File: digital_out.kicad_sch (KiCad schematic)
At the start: 2 parts, among them U5 AM26LS31

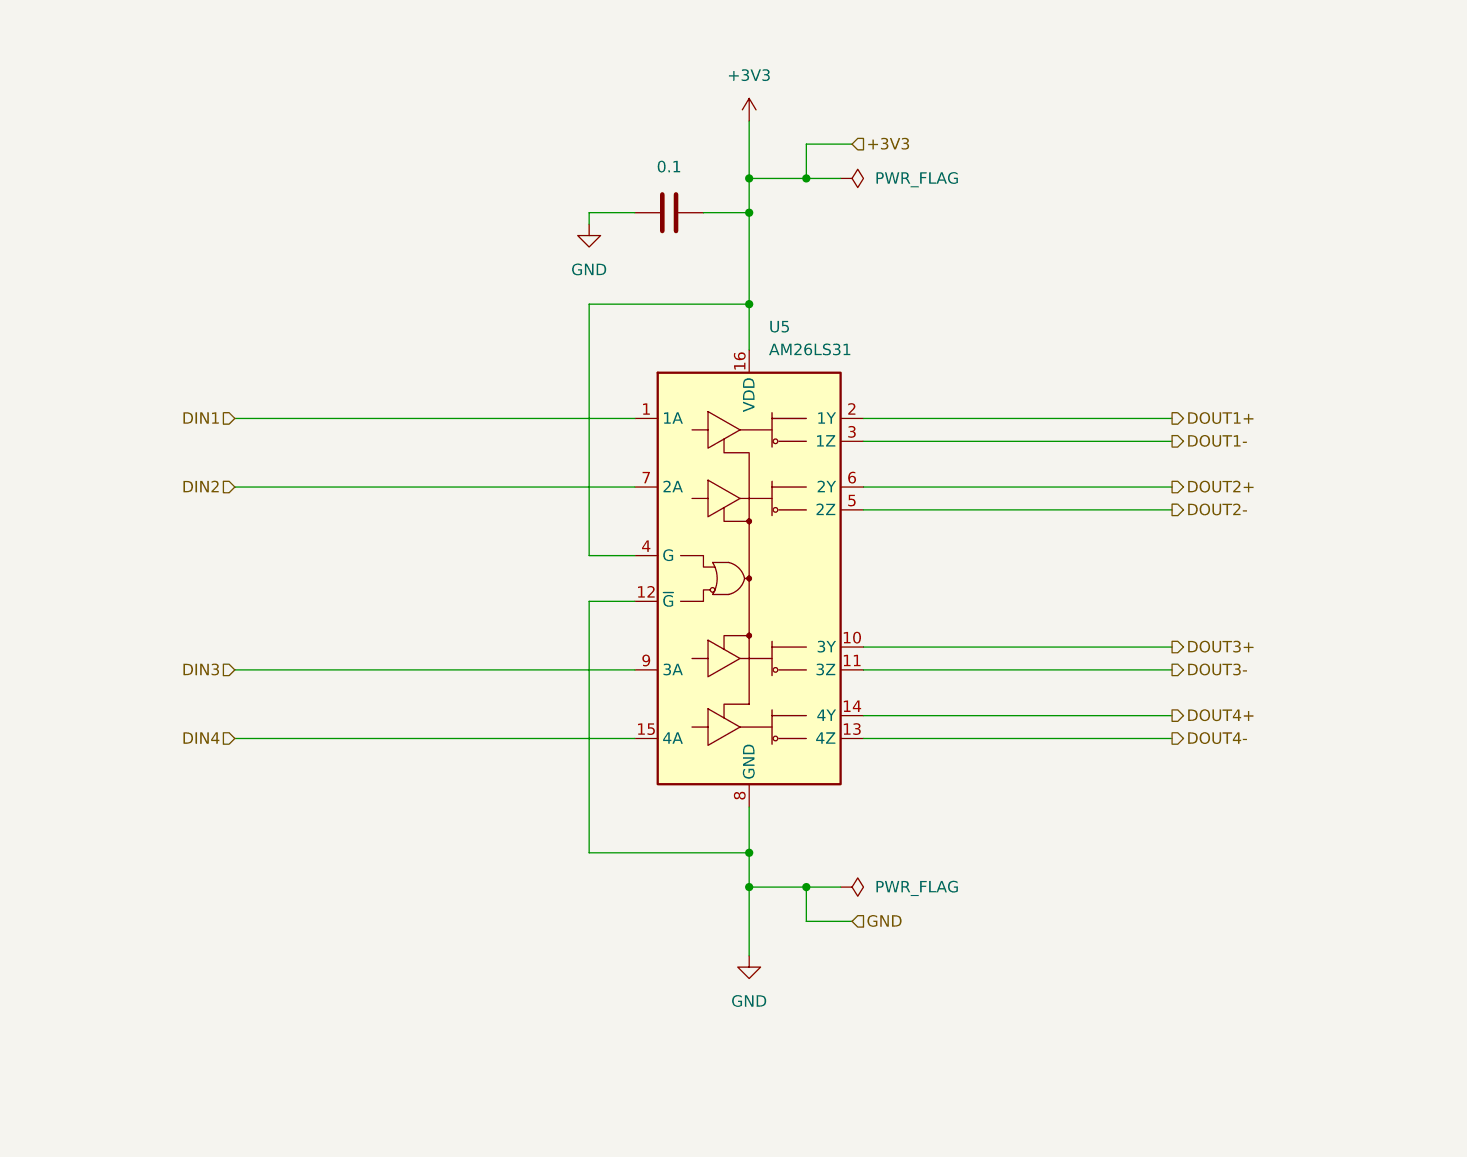
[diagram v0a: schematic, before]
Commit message: Finished power setup and cleared some mistakes
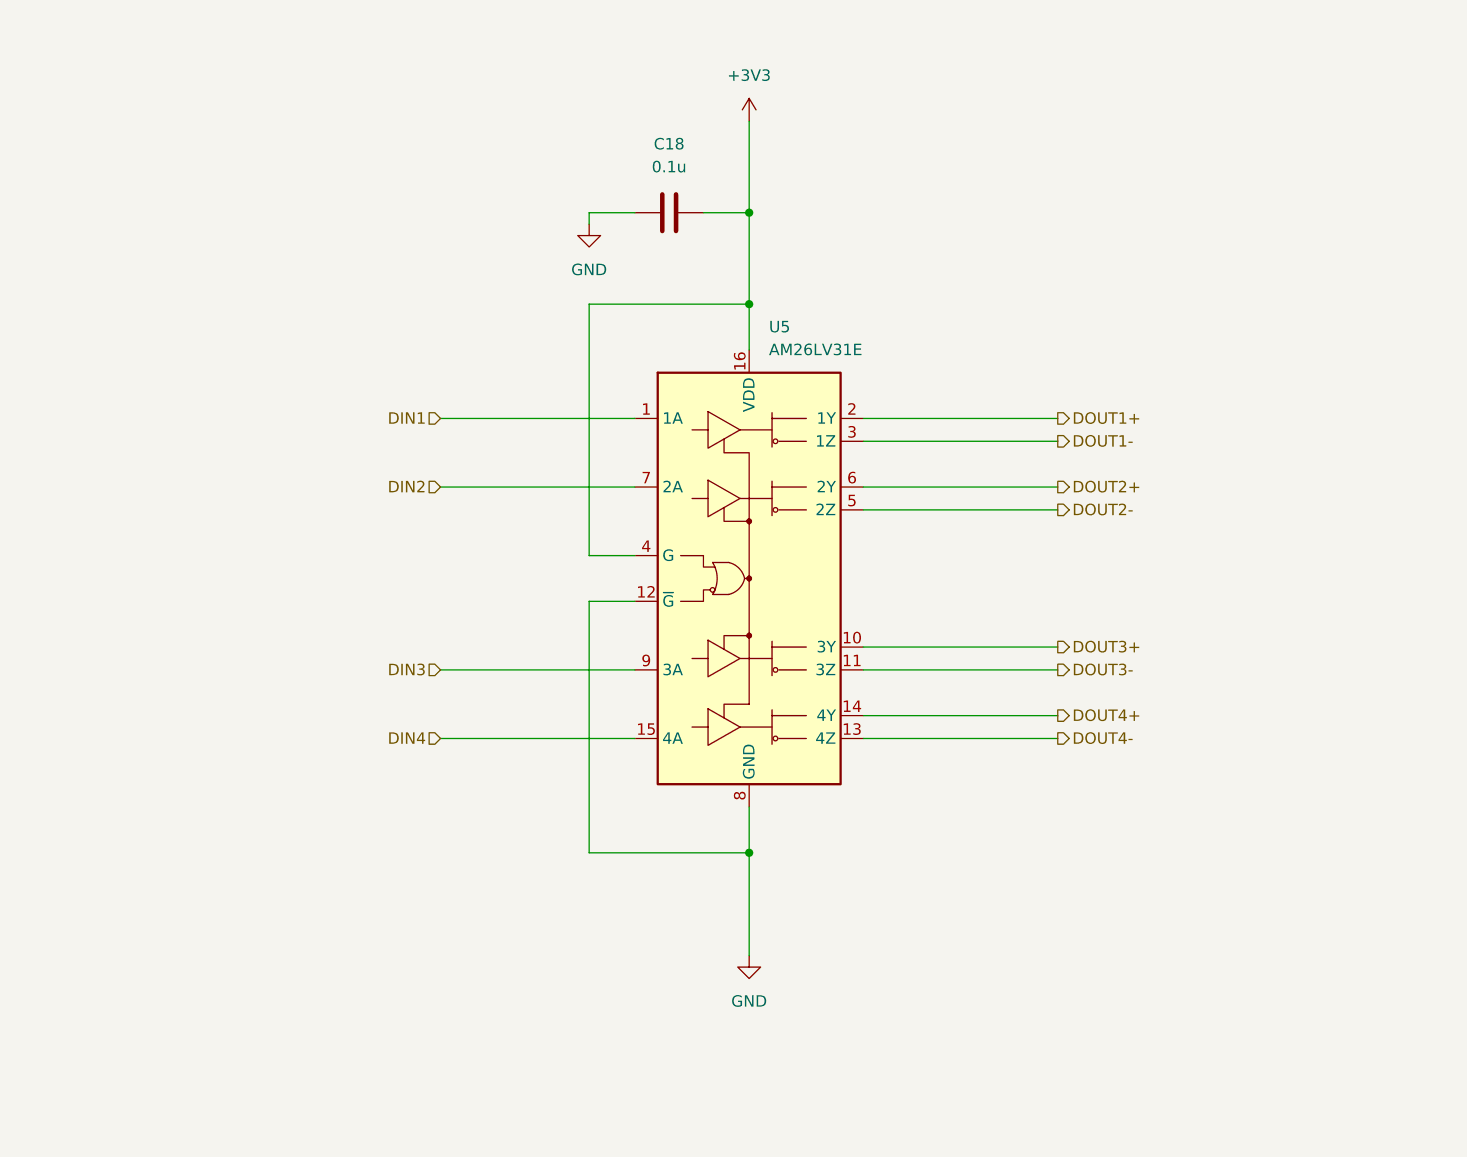
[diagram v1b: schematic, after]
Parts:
- C18: value 0.1 -> 0.1u
- U5: value AM26LS31 -> AM26LV31E

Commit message: Assigned proper footprints for all components
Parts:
- C18: value 0.1u -> 100n; footprint (none) -> Capacitor_SMD:C_0603_1608Metric_Pad1.08x0.95mm_HandSolder
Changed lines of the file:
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@@
       (effects (font (size 1.27 1.27)))
     )
-    (property "Value" "0.1u" (at 146.05 45.72 90)
+    (property "Value" "100n" (at 146.05 45.72 90)
       (effects (font (size 1.27 1.27)))
     )
-    (property "Footprint" "" (at 149.86 49.8348 0)
+    (property "Footprint" "Capacitor_SMD:C_0603_1608Metric_Pad1.08x0.95mm_HandSolder" (at 149.86 49.8348 0)
       (effects (font (size 1.27 1.27)) hide)
     )

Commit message: Finished annotation
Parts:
- renumbered C18 to C2601, U5 to U2601
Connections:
- net DOUT1+ renamed DIN1+
- net DOUT1- renamed DIN1-
- net DOUT2+ renamed DIN2+
- net DOUT2- renamed DIN2-
- net DOUT3+ renamed DIN3+
- net DOUT3- renamed DIN3-
- net DOUT4+ renamed DIN4+
- net DOUT4- renamed DIN4-

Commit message: Merged receiver and transmitter
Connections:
- net DIN1 renamed DOUT1
- net DIN1+ renamed DOUT1+
- net DIN1- renamed DOUT1-
- net DIN2 renamed DOUT2
- net DIN2+ renamed DOUT2+
- net DIN2- renamed DOUT2-
- net DIN3 renamed DOUT3
- net DIN3+ renamed DOUT3+
- net DIN3- renamed DOUT3-
- net DIN4 renamed DOUT4
- net DIN4+ renamed DOUT4+
- net DIN4- renamed DOUT4-
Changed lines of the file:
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@@
     (stroke (width 0) (type default))
   )
-  (hierarchical_label "DIN3-" (shape output) (at 189.23 101.6 0) (fields_autoplaced)
+  (hierarchical_label "DOUT3-" (shape output) (at 189.23 101.6 0) (fields_autoplaced)
     (effects (font (size 1.27 1.27)) (justify left))
   )
-  (hierarchical_label "DIN1-" (shape output) (at 189.23 76.2 0) (fields_autoplaced)
+  (hierarchical_label "DOUT1-" (shape output) (at 189.23 76.2 0) (fields_autoplaced)
     (effects (font (size 1.27 1.27)) (justify left))
   )
-  (hierarchical_label "DIN4" (shape input) (at 120.65 109.22 180) (fields_autoplaced)
+  (hierarchical_label "DOUT4" (shape input) (at 120.65 109.22 180) (fields_autoplaced)
     (effects (font (size 1.27 1.27)) (justify right))
   )
-  (hierarchical_label "DIN2-" (shape output) (at 189.23 83.82 0) (fields_autoplaced)
+  (hierarchical_label "DOUT2-" (shape output) (at 189.23 83.82 0) (fields_autoplaced)
     (effects (font (size 1.27 1.27)) (justify left))
   )
-  (hierarchical_label "DIN3" (shape input) (at 120.65 101.6 180) (fields_autoplaced)
+  (hierarchical_label "DOUT3" (shape input) (at 120.65 101.6 180) (fields_autoplaced)
     (effects (font (size 1.27 1.27)) (justify right))
   )
-  (hierarchical_label "DIN4+" (shape output) (at 189.23 106.68 0) (fields_autoplaced)
+  (hierarchical_label "DOUT4+" (shape output) (at 189.23 106.68 0) (fields_autoplaced)
     (effects (font (size 1.27 1.27)) (justify left))
   )
-  (hierarchical_label "DIN3+" (shape output) (at 189.23 99.06 0) (fields_autoplaced)
+  (hierarchical_label "DOUT3+" (shape output) (at 189.23 99.06 0) (fields_autoplaced)
     (effects (font (size 1.27 1.27)) (justify left))
   )
-  (hierarchical_label "DIN2" (shape input) (at 120.65 81.28 180) (fields_autoplaced)
+  (hierarchical_label "DOUT2" (shape input) (at 120.65 81.28 180) (fields_autoplaced)
     (effects (font (size 1.27 1.27)) (justify right))
   )
-  (hierarchical_label "DIN1" (shape input) (at 120.65 73.66 180) (fields_autoplaced)
+  (hierarchical_label "DOUT1" (shape input) (at 120.65 73.66 180) (fields_autoplaced)
     (effects (font (size 1.27 1.27)) (justify right))
   )
-  (hierarchical_label "DIN4-" (shape output) (at 189.23 109.22 0) (fields_autoplaced)
+  (hierarchical_label "DOUT4-" (shape output) (at 189.23 109.22 0) (fields_autoplaced)
     (effects (font (size 1.27 1.27)) (justify left))
   )
-  (hierarchical_label "DIN1+" (shape output) (at 189.23 73.66 0) (fields_autoplaced)
+  (hierarchical_label "DOUT1+" (shape output) (at 189.23 73.66 0) (fields_autoplaced)
     (effects (font (size 1.27 1.27)) (justify left))
   )
-  (hierarchical_label "DIN2+" (shape output) (at 189.23 81.28 0) (fields_autoplaced)
+  (hierarchical_label "DOUT2+" (shape output) (at 189.23 81.28 0) (fields_autoplaced)
     (effects (font (size 1.27 1.27)) (justify left))
   )

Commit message: Fixed ERC errors and warnings
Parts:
- added R2001, R2003, R2005, R2007, R2010, R2011, R2014, R2015: 0, Resistor_SMD:R_0603_1608Metric_Pad0.98x0.95mm_HandSolder, symbol Device:R
- added R2002, R2004, R2006, R2008, R2009, R2012, R2013, R2016: 10, Resistor_SMD:R_0603_1608Metric_Pad0.98x0.95mm_HandSolder, symbol Device:R
- added U2001, U2003: CDSOT236-T05, Package_TO_SOT_SMD:SOT-23-6, symbol Power_Protection:CDSOT236-0504C
- renumbered U2601 to U2602
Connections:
- net DOUT1: now also R2001.1; no longer U2602.1 (1A)
- net DOUT1+: now also R2002.2; no longer U2602.2 (1Y)
- net DOUT1-: now also R2004.2; no longer U2602.3 (1Z)
- net DOUT2: now also R2005.1; no longer U2602.7 (2A)
- net DOUT2+: now also R2006.2; no longer U2602.6 (2Y)
- net DOUT2-: now also R2008.2; no longer U2602.5 (2Z)
- net DOUT3: now also R2010.1; no longer U2602.9 (3A)
- net DOUT3+: now also R2009.2; no longer U2602.10 (3Y)
- net DOUT3-: now also R2012.2; no longer U2602.11 (3Z)
- net DOUT4: now also R2014.1; no longer U2602.15 (4A)
- net DOUT4+: now also R2013.2; no longer U2602.14 (4Y)
- net DOUT4-: now also R2016.2; no longer U2602.13 (4Z)
- net GND: now also U2001.2 (VN), U2003.2 (VN)
- new net: R2011.1, U2602.11 (3Z)
- new net: R2011.2, R2012.1, U2003.3 (IO2)
- new net: R2014.2, U2602.15 (4A)
- new net: R2006.1, U2001.4 (IO3), U2602.6 (2Y)
- new net: R2005.2, U2602.7 (2A)
- new net: R2007.1, U2602.5 (2Z)
- new net: R2007.2, R2008.1, U2001.6 (IO4)
- new net: R2001.2, U2602.1 (1A)
- new net: R2003.1, U2602.3 (1Z)
- new net: R2003.2, R2004.1, U2001.3 (IO2)
- new net: R2009.1, U2003.1 (IO1), U2602.10 (3Y)
- new net: R2013.1, U2003.4 (IO3), U2602.14 (4Y)
- new net: R2015.2, R2016.1, U2003.6 (IO4)
- new net: R2015.1, U2602.13 (4Z)
- new net: R2002.1, U2001.1 (IO1), U2602.2 (1Y)
- new net: R2010.2, U2602.9 (3A)
- no-connect marks 0 -> 2
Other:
- moved on the sheet: C2601, U2602

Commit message: Split schematic into three subprojects
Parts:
- renumbered C2601 to C42, R2001 to R106, R2002 to R107, R2003 to R108, R2004 to R109, R2005 to R110, R2006 to R111, R2007 to R112, R2008 to R113, R2009 to R114, R2010 to R115, R2011 to R116, R2012 to R117, R2013 to R118, R2014 to R119, R2015 to R120, R2016 to R121, U2001 to U20, U2602 to U21, U2003 to U22

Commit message: Updated designators positions
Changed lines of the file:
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@@
   (symbol (lib_id "Device:R") (at 146.05 101.6 90) (unit 1)
     (in_bom yes) (on_board yes) (dnp no)
-    (property "Reference" "R116" (at 146.05 95.25 90)
-      (effects (font (size 1.27 1.27)) hide)
+    (property "Reference" "R116" (at 151.13 100.33 90)
+      (effects (font (size 1.27 1.27)))
     )
     (property "Value" "0" (at 146.05 101.6 90)
@@
   (symbol (lib_id "Device:R") (at 92.71 109.22 90) (unit 1)
     (in_bom yes) (on_board yes) (dnp no)
-    (property "Reference" "R119" (at 92.71 102.87 90)
-      (effects (font (size 1.27 1.27)) hide)
+    (property "Reference" "R119" (at 92.71 107.188 90)
+      (effects (font (size 1.27 1.27)))
     )
     (property "Value" "0" (at 92.71 109.22 90)
@@
   (symbol (lib_id "Device:R") (at 209.55 81.28 90) (unit 1)
     (in_bom yes) (on_board yes) (dnp no)
-    (property "Reference" "R111" (at 209.55 74.93 90)
-      (effects (font (size 1.27 1.27)) hide)
+    (property "Reference" "R111" (at 214.63 80.01 90)
+      (effects (font (size 1.27 1.27)))
     )
     (property "Value" "10" (at 209.55 81.28 90)
@@
   (symbol (lib_id "Device:R") (at 92.71 81.28 90) (unit 1)
     (in_bom yes) (on_board yes) (dnp no)
-    (property "Reference" "R110" (at 92.71 74.93 90)
-      (effects (font (size 1.27 1.27)) hide)
+    (property "Reference" "R110" (at 92.71 79.248 90)
+      (effects (font (size 1.27 1.27)))
     )
     (property "Value" "0" (at 92.71 81.28 90)
@@
   (symbol (lib_id "Device:R") (at 146.05 83.82 90) (unit 1)
     (in_bom yes) (on_board yes) (dnp no)
-    (property "Reference" "R112" (at 146.05 77.47 90)
-      (effects (font (size 1.27 1.27)) hide)
+    (property "Reference" "R112" (at 151.13 82.55 90)
+      (effects (font (size 1.27 1.27)))
     )
     (property "Value" "0" (at 146.05 83.82 90)
@@
   (symbol (lib_id "Device:R") (at 92.71 73.66 90) (unit 1)
     (in_bom yes) (on_board yes) (dnp no)
-    (property "Reference" "R106" (at 92.71 67.31 90)
-      (effects (font (size 1.27 1.27)) hide)
+    (property "Reference" "R106" (at 92.71 71.628 90)
+      (effects (font (size 1.27 1.27)))
     )
     (property "Value" "0" (at 92.71 73.66 90)
@@
   (symbol (lib_id "Device:R") (at 146.05 76.2 90) (unit 1)
     (in_bom yes) (on_board yes) (dnp no)
-    (property "Reference" "R108" (at 146.05 69.85 90)
-      (effects (font (size 1.27 1.27)) hide)
+    (property "Reference" "R108" (at 151.13 74.93 90)
+      (effects (font (size 1.27 1.27)))
     )
     (property "Value" "0" (at 146.05 76.2 90)
@@
   (symbol (lib_id "Device:R") (at 146.05 109.22 90) (unit 1)
     (in_bom yes) (on_board yes) (dnp no)
-    (property "Reference" "R120" (at 146.05 102.87 90)
-      (effects (font (size 1.27 1.27)) hide)
+    (property "Reference" "R120" (at 151.13 107.95 90)
+      (effects (font (size 1.27 1.27)))
     )
     (property "Value" "0" (at 146.05 109.22 90)
@@
   (symbol (lib_id "Device:R") (at 209.55 101.6 90) (unit 1)
     (in_bom yes) (on_board yes) (dnp no)
-    (property "Reference" "R117" (at 209.55 95.25 90)
-      (effects (font (size 1.27 1.27)) hide)
+    (property "Reference" "R117" (at 214.63 100.33 90)
+      (effects (font (size 1.27 1.27)))
     )
     (property "Value" "10" (at 209.55 101.6 90)
@@
   (symbol (lib_id "Device:R") (at 209.55 106.68 90) (unit 1)
     (in_bom yes) (on_board yes) (dnp no)
-    (property "Reference" "R118" (at 209.55 100.33 90)
-      (effects (font (size 1.27 1.27)) hide)
+    (property "Reference" "R118" (at 214.63 105.41 90)
+      (effects (font (size 1.27 1.27)))
     )
     (property "Value" "10" (at 209.55 106.68 90)
@@
   (symbol (lib_id "Device:R") (at 209.55 73.66 90) (unit 1)
     (in_bom yes) (on_board yes) (dnp no)
-    (property "Reference" "R107" (at 209.55 67.31 90)
-      (effects (font (size 1.27 1.27)) hide)
+    (property "Reference" "R107" (at 214.63 72.39 90)
+      (effects (font (size 1.27 1.27)))
     )
     (property "Value" "10" (at 209.55 73.66 90)
@@
   (symbol (lib_id "Device:R") (at 92.71 101.6 90) (unit 1)
     (in_bom yes) (on_board yes) (dnp no)
-    (property "Reference" "R115" (at 92.71 95.25 90)
-      (effects (font (size 1.27 1.27)) hide)
+    (property "Reference" "R115" (at 92.71 99.568 90)
+      (effects (font (size 1.27 1.27)))
     )
     (property "Value" "0" (at 92.71 101.6 90)
@@
   (symbol (lib_id "Device:R") (at 209.55 109.22 90) (unit 1)
     (in_bom yes) (on_board yes) (dnp no)
-    (property "Reference" "R121" (at 209.55 102.87 90)
-      (effects (font (size 1.27 1.27)) hide)
+    (property "Reference" "R121" (at 214.63 107.95 90)
+      (effects (font (size 1.27 1.27)))
     )
     (property "Value" "10" (at 209.55 109.22 90)
@@
   (symbol (lib_id "Device:R") (at 209.55 83.82 90) (unit 1)
     (in_bom yes) (on_board yes) (dnp no)
-    (property "Reference" "R113" (at 209.55 77.47 90)
-      (effects (font (size 1.27 1.27)) hide)
+    (property "Reference" "R113" (at 214.63 82.55 90)
+      (effects (font (size 1.27 1.27)))
     )
     (property "Value" "10" (at 209.55 83.82 90)
@@
   (symbol (lib_id "Device:R") (at 209.55 76.2 90) (unit 1)
     (in_bom yes) (on_board yes) (dnp no)
-    (property "Reference" "R109" (at 209.55 69.85 90)
-      (effects (font (size 1.27 1.27)) hide)
+    (property "Reference" "R109" (at 214.63 74.93 90)
+      (effects (font (size 1.27 1.27)))
     )
     (property "Value" "10" (at 209.55 76.2 90)
@@
   (symbol (lib_id "Device:R") (at 209.55 99.06 90) (unit 1)
     (in_bom yes) (on_board yes) (dnp no)
-    (property "Reference" "R114" (at 209.55 92.71 90)
-      (effects (font (size 1.27 1.27)) hide)
+    (property "Reference" "R114" (at 214.63 97.79 90)
+      (effects (font (size 1.27 1.27)))
     )
     (property "Value" "10" (at 209.55 99.06 90)
